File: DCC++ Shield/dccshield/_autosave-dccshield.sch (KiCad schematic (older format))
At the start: 29 parts, among them J1 Conn_01x06, Q1 BTN8982TA, Q2 BTN8982TA, U1 74HC04, U2 A4953_LJ, U3 LM358

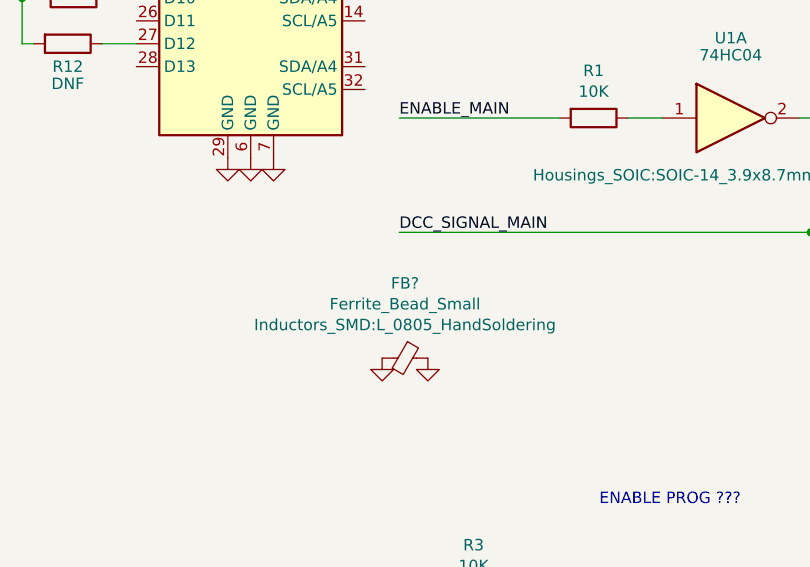
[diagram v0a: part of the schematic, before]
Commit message: 3d models added
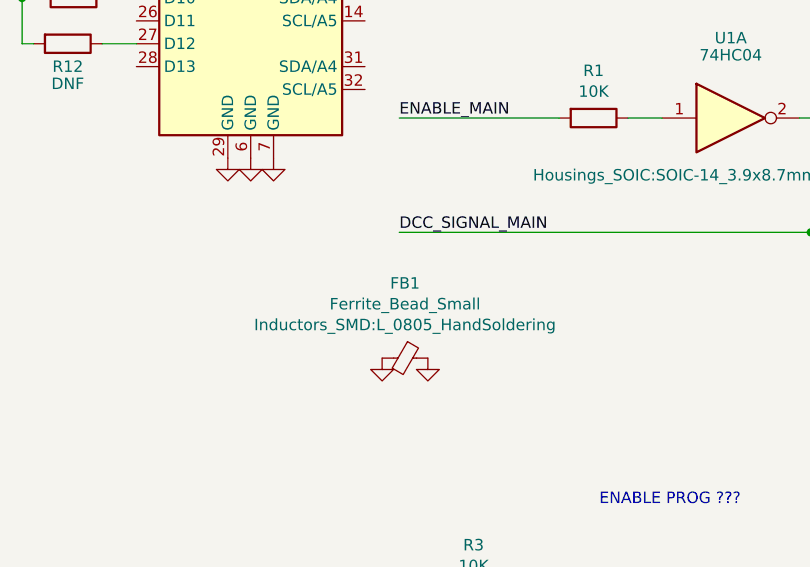
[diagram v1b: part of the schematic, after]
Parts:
- gave numbers to parts that had none: 1
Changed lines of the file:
@@
 	2100 2450 2225 2450
 $Comp
-L Device:Ferrite_Bead_Small FB?
+L Device:Ferrite_Bead_Small FB1
 U 1 1 5E3E685D
 P 3400 4025
-F 0 "FB?" V 3073 4025 50  0000 C CNN
+F 0 "FB1" V 3073 4025 50  0000 C CNN
 F 1 "Ferrite_Bead_Small" V 3164 4025 50  0000 C CNN
 F 2 "Inductors_SMD:L_0805_HandSoldering" V 3255 4025 50  0000 C CNN
@@
 $EndComp
 $Comp
-L power:GND #PWR?
+L power:GND #PWR0122
 U 1 1 5E3E774A
 P 3300 4025
-F 0 "#PWR?" H 3300 3775 50  0001 C CNN
+F 0 "#PWR0122" H 3300 3775 50  0001 C CNN
 F 1 "GND" H 3305 3852 50  0001 C CNN
 F 2 "" H 3300 4025 50  0001 C CNN
@@
 $EndComp
 $Comp
-L power:GND #PWR?
+L power:GND #PWR0123
 U 1 1 5E3E7E28
 P 3500 4025
-F 0 "#PWR?" H 3500 3775 50  0001 C CNN
+F 0 "#PWR0123" H 3500 3775 50  0001 C CNN
 F 1 "GND" H 3505 3852 50  0001 C CNN
 F 2 "" H 3500 4025 50  0001 C CNN
